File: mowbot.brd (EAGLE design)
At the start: 100 x 80 mm, 20 parts, among them Q1 PSMN9R1-30YL-MOSFET_N, Q2 PSMN9R1-30YL-MOSFET_N, Q3 PSMN9R1-30YL-MOSFET_N, Q4 PSMN9R1-30YL-MOSFET_N, Q5 PSMN9R1-30YL-MOSFET_N, Q6 PSMN9R1-30YL-MOSFET_N, Q7 PSMN9R1-30YL-MOSFET_N, Q8 PSMN9R1-30YL-MOSFET_N

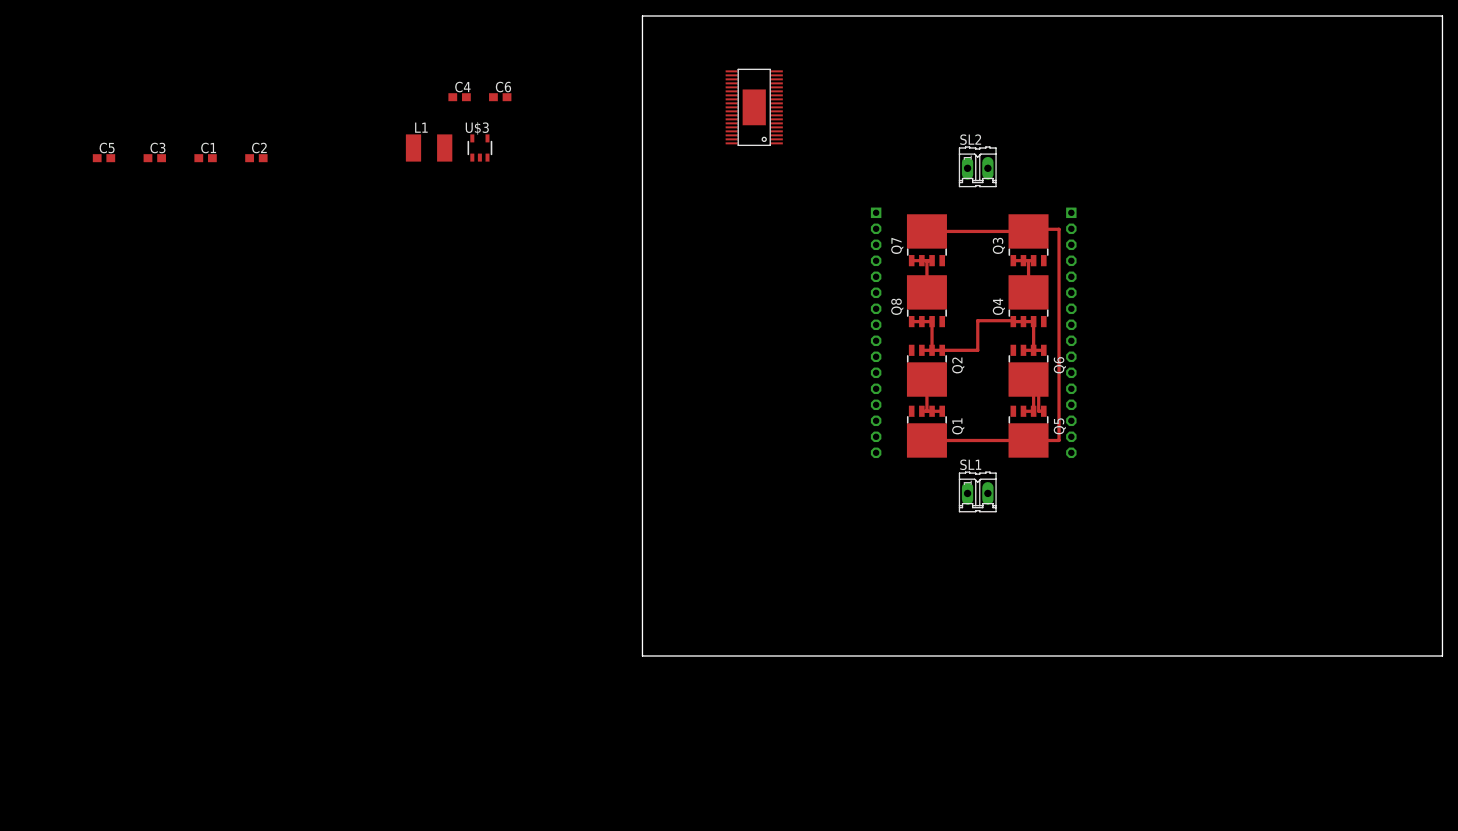
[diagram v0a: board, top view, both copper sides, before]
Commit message: Arranged power FETs
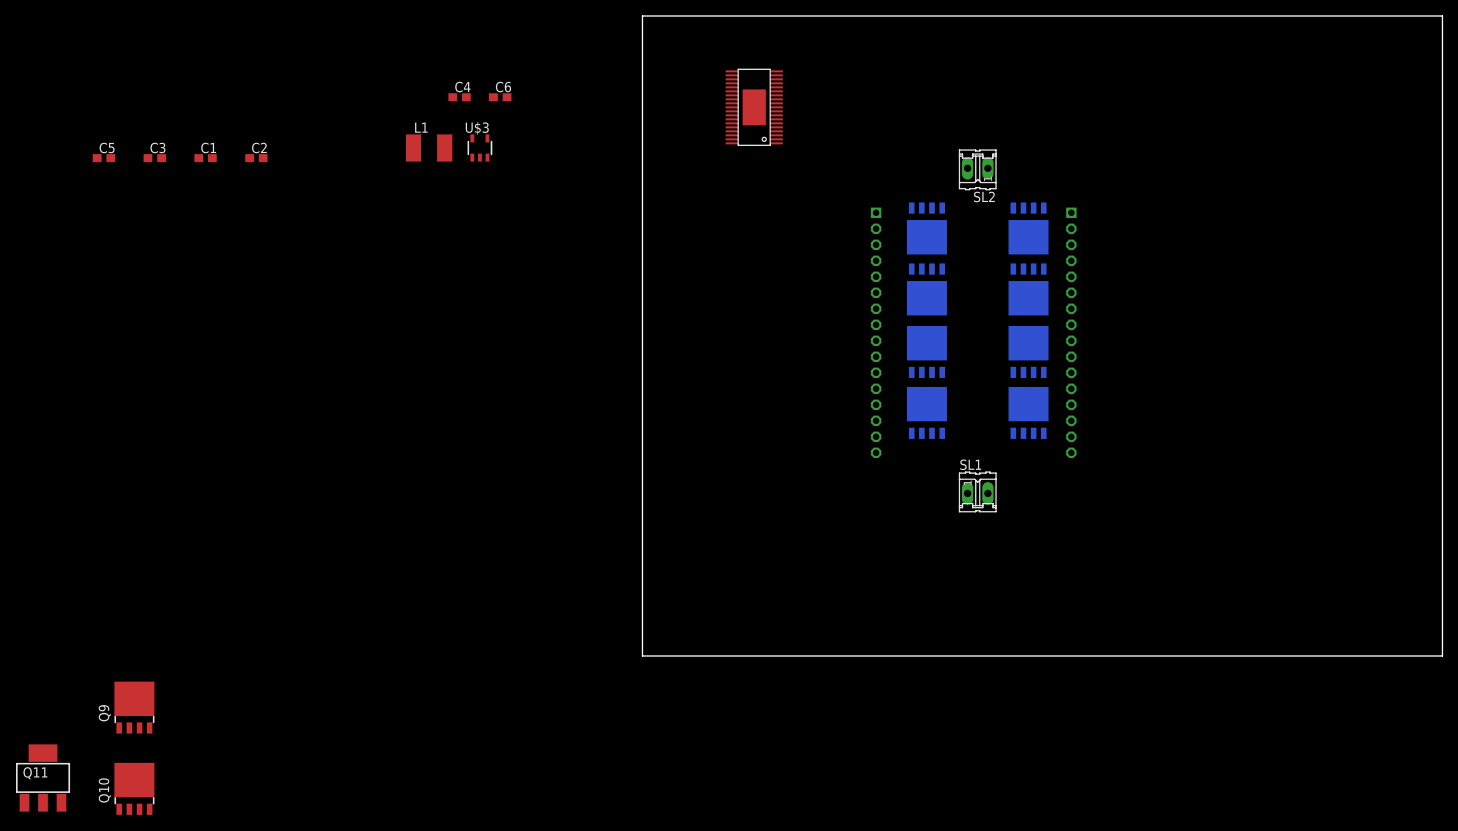
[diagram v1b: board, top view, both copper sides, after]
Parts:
- added Q10, Q9: PSMN9R1-30YL-MOSFET_N, PSMN9R1-30YL_MOSFET_N:SOT669
- added Q11: N-HEXFET_SOT323-, transistor-power:SOT223
- moved Q1 10.2 mm to (35.6, 38.1), flipped to the bottom, turned to 0 degrees
- moved Q5 10.2 mm to (48.3, 38.1), flipped to the bottom, turned to 0 degrees
- moved Q4 8.89 mm to (48.3, 53.3), flipped to the bottom, turned to 180 degrees
- moved Q8 8.89 mm to (35.6, 53.3), flipped to the bottom, turned to 180 degrees
- moved Q3 6.35 mm to (48.3, 45.7), flipped to the bottom, turned to 180 degrees
- moved Q7 6.35 mm to (35.6, 45.7), flipped to the bottom, turned to 180 degrees
- moved Q2 5.08 mm to (35.6, 30.5), flipped to the bottom, turned to 0 degrees
- moved Q6 5.08 mm to (48.3, 30.5), flipped to the bottom, turned to 0 degrees
- turned SL2 to 180 degrees
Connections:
- removed net N$7: C4.1, U$1.3
- new net N$2: C4.2, U$1.3
- new net N$4: Q4.1, Q4.2, Q4.3, Q8.1, Q8.2, Q8.3, Q9.MB
- new net N$9: Q10.MB, Q2.1, Q2.2, Q2.3, Q6.1, Q6.2, Q6.3
- net +12V: now also C2.1, C3.1, C4.1, Q10.4, Q11.1, Q9.4; no longer C2.2, C3.2, C4.2
- net GND: now also C2.2, C3.2, Q10.1, Q10.2, Q10.3, Q11.3, Q11.4, Q9.1, Q9.2, Q9.3; no longer C2.1, C3.1, Q2.1, Q2.2, Q2.3, Q4.1, Q4.2, Q4.3, Q6.1, Q6.2, Q6.3, Q8.1, Q8.2, Q8.3
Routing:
- net +12V: track 59.7 -> 0.00 mm
- net GND: track 30.0 -> 0.00 mm
- net AOUT1: track 13.8 -> 0.00 mm
- net BOUT1: track 7.14 -> 0.00 mm
- net AOUT2: track 6.51 -> 0.00 mm
- net BOUT2: track 6.51 -> 0.00 mm

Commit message: Added reverse battery protection
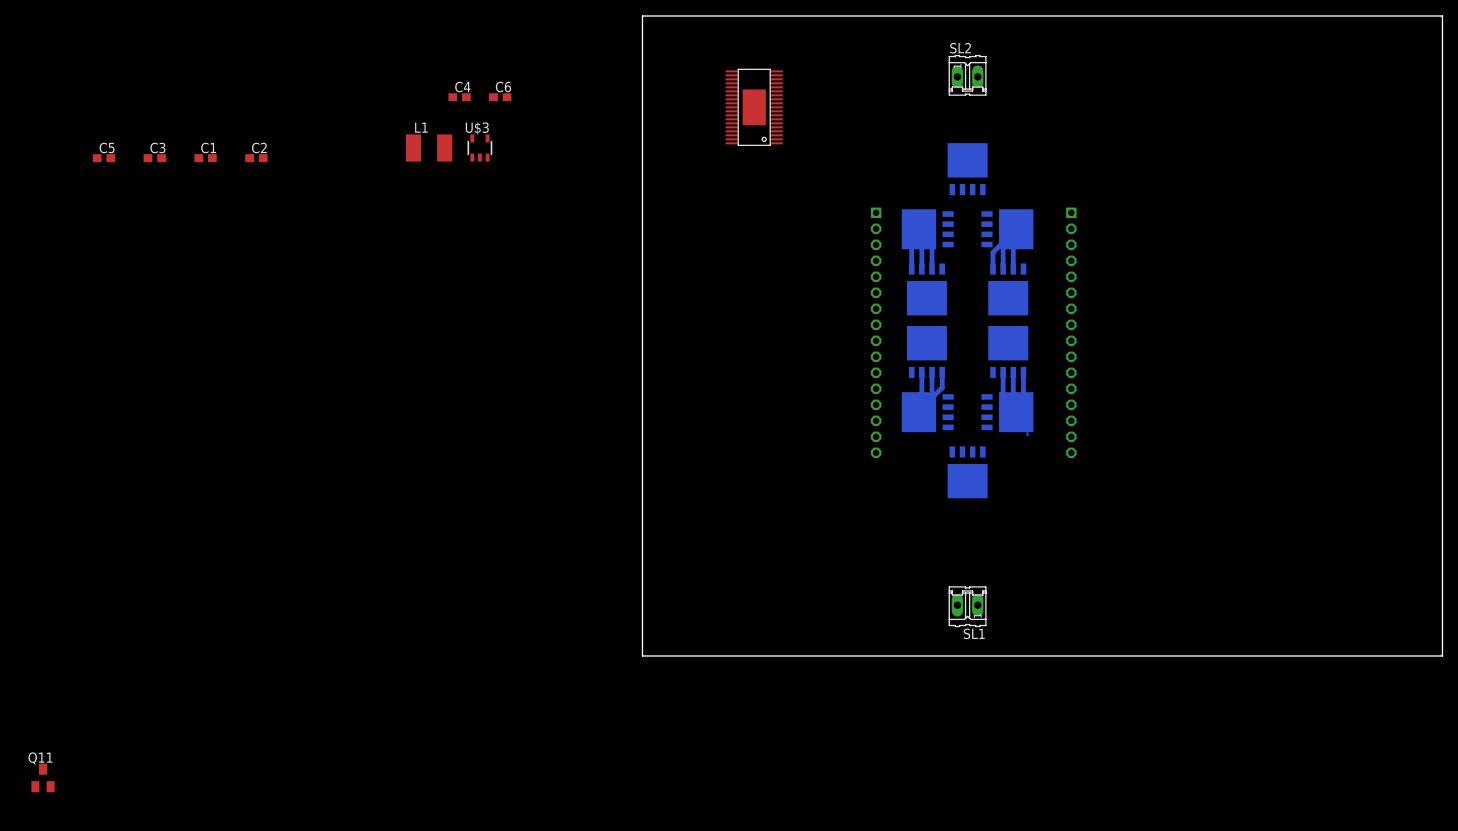
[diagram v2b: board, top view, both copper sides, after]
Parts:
- Q11: value N-HEXFET_SOT323- -> DMG2302UK-NMOSFET; device transistor-power:SOT223 -> DMG2302UK_NMOSFET:SOT23
- moved Q9 124.0 mm to (40.6, 61.0), flipped to the bottom
- moved Q10 111.3 mm to (40.6, 22.9), flipped to the bottom, turned to 180 degrees
- moved SL1 14.0 mm to (40.6, 6.35), turned to 180 degrees
- moved SL2 11.5 mm to (40.6, 72.4), turned to 0 degrees
- moved Q3 2.54 mm to (45.7, 45.7)
- moved Q4 2.54 mm to (45.7, 53.3), turned to 90 degrees
- moved Q5 2.54 mm to (45.7, 38.1)
- moved Q6 2.54 mm to (45.7, 30.5), turned to 90 degrees
- turned Q2 to 270 degrees
- turned Q8 to 270 degrees
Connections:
- net GND: now also Q10.MB, Q11.2, Q9.MB; no longer Q10.1, Q10.2, Q10.3, Q11.4, Q9.1, Q9.2, Q9.3
- net N$4: now also Q9.1, Q9.2, Q9.3; no longer Q9.MB
- net N$9: now also Q10.1, Q10.2, Q10.3; no longer Q10.MB
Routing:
- net BOUT2: track 0.00 -> 16.9 mm
- net AOUT1: track 0.00 -> 16.1 mm
- net BOUT1: track 0.00 -> 15.6 mm
- net AOUT2: track 0.00 -> 14.5 mm

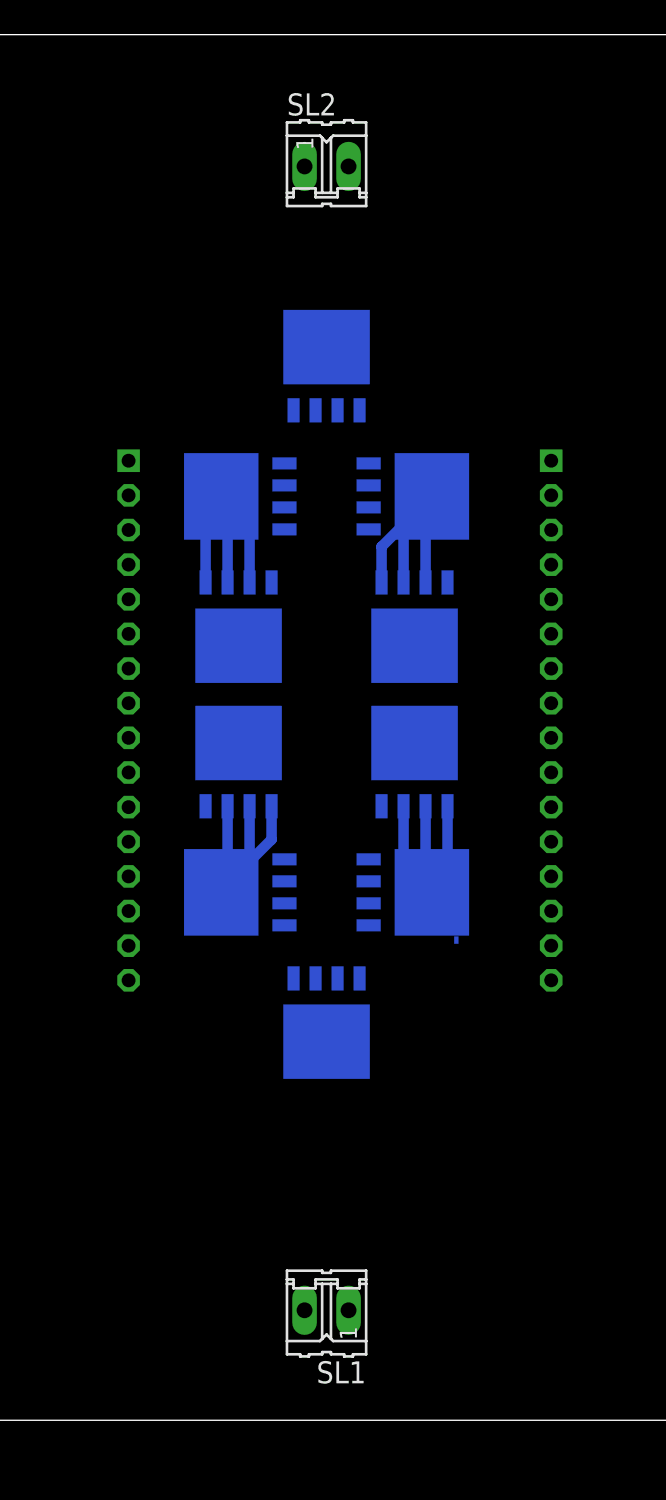
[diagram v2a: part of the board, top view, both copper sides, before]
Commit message: replaced fets and routed them
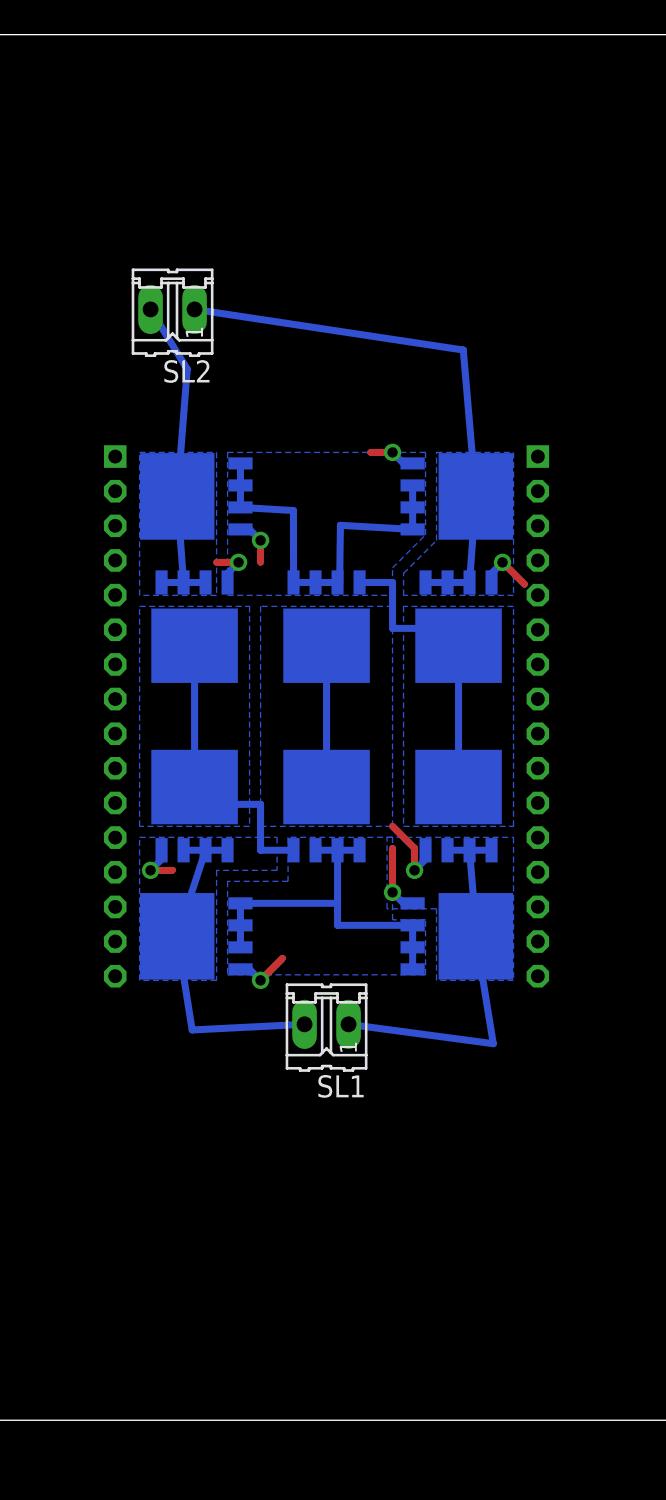
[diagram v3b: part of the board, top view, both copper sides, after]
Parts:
- moved U$2 19.1 mm to (40.6, 40.6)
- moved SL1 16.5 mm to (40.6, 22.9)
- moved Q9 15.2 mm to (40.6, 45.7), turned to 180 degrees
- moved Q10 12.7 mm to (40.6, 35.6), turned to 0 degrees
- moved Q3 12.7 mm to (33.0, 45.7)
- moved Q4 12.7 mm to (33.0, 53.3), turned to 270 degrees
- moved Q7 12.7 mm to (48.3, 45.7)
- moved Q8 12.7 mm to (48.3, 53.3), turned to 90 degrees
- moved SL2 12.1 mm to (31.8, 64.1), turned to 180 degrees
- moved Q1 3.59 mm to (33.0, 35.6)
- moved Q2 3.59 mm to (33.0, 27.9)
- moved Q5 3.59 mm to (48.3, 35.6)
- moved Q6 3.59 mm to (48.3, 27.9)
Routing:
- net +12V: track 0.00 -> 35.0 mm
- net N$4: track 0.00 -> 22.6 mm
- net N$9: track 0.00 -> 21.9 mm
- net BOUT1: track 15.6 -> 31.7 mm
- net GND: track 0.00 -> 9.16 mm
- net AOUT1: track 16.1 -> 22.8 mm
- net AOUT2: track 14.5 -> 19.7 mm
- net A1HS: track 0.00 -> 4.49 mm, vias 0 -> 1
- net A1LS: track 0.00 -> 3.96 mm, vias 0 -> 1
- net B1HS: track 0.00 -> 3.22 mm, vias 0 -> 1
- net A2LS: track 0.00 -> 3.22 mm, vias 0 -> 1
- net B2HS: track 0.00 -> 2.69 mm, vias 0 -> 1
- net B1LS: track 0.00 -> 2.69 mm, vias 0 -> 1
- net B2LS: track 0.00 -> 2.69 mm, vias 0 -> 1
- net A2HS: track 0.00 -> 2.69 mm, vias 0 -> 1
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- added copper zone on layer 16, net +12V
- added copper zone on layer 16, net AOUT1
- added copper zone on layer 16, net AOUT2
- added copper zone on layer 16, net BOUT1
- added copper zone on layer 16, net BOUT2
- added copper zone on layer 16, net GND
- added copper zone on layer 16, net N$4
- added copper zone on layer 16, net N$9
